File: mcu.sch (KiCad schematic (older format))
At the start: 73 parts, among them J10 JTAG, J11 esp32L, J12 esp32B, J13 esp32R, J2 SPI1, J3 uSD, J4 I2C1, J5 serial1, J6 serial2, J7 touch interface, J8 LCD 4.3, J9 EXT_IOS, Q1 ZXMN2F30FH, Q2 ZXMN2F30FH, Q3 ZXMN2F30FH, SW1 reset, SW7 on, U3 AT25SF641, U5 STM32F750Z8, U6 MP3302DJ-LF-P, U7 ESP32-WROOM-32, Y1 25MHz, Y2 32.768 kHz

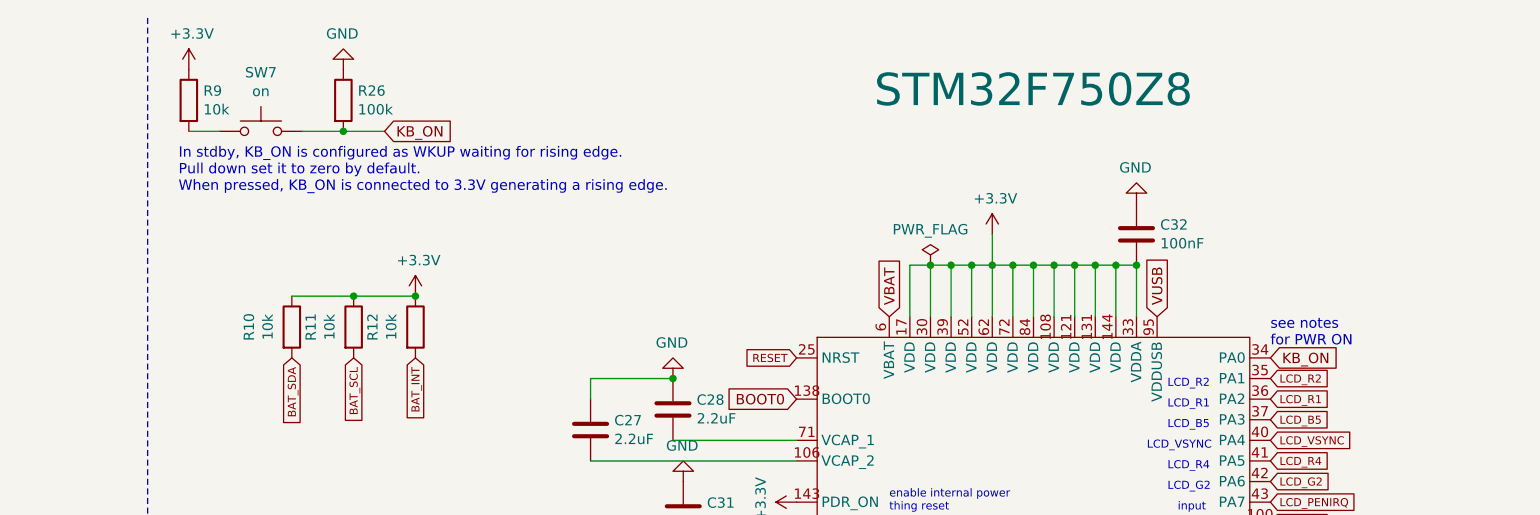
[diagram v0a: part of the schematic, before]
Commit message: fix wakeup
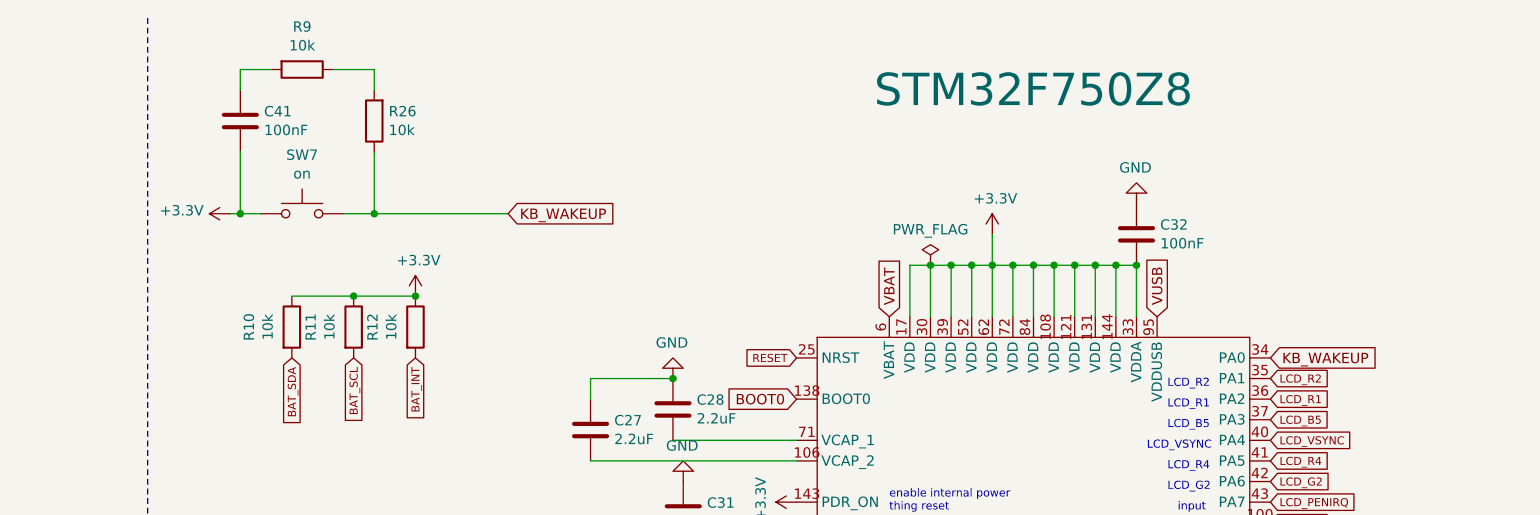
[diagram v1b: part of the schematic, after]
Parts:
- added C41: 100nF, Capacitor_SMD:C_0805_2012Metric_Pad1.18x1.45mm_HandSolder, symbol Device:C
- R26: value 100k -> 10k
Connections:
- net +3V3: now also SW7.1, C41.1; no longer R9.1
- net GND: no longer R26.1
- net at R9.2: now also C41.2; no longer SW7.1
- net KB_ON renamed KB_WAKEUP
- net KB_WAKEUP: now also R26.1; no longer R26.2
- new net: R26.2, R9.1
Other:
- note removed: "In stdby, KB_ON is configured as WKUP waiting for rising edge.\nPull down set it to zero by default.\nWhen pressed, KB_ON is connected to 3.3V generating a rising edge."
- note removed: "see notes\nfor PWR ON"
- moved on the sheet: SW7
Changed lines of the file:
@@
 KB_ROW_10
 Text GLabel 15050 2150 2    50   Input ~ 0
-KB_ON
+KB_WAKEUP
 Text Notes 3750 10750 0    118  ~ 0
 PWR On button is KB_COL_1 / KB_ROW_11\nESC button is KB_COL_12 / KB_ROW_1
@@
 Text Notes 600  11100 0    98   ~ 0
 TODO to validate:\n- BOOT0 behavior\n- WAKEUP through ON behavior\n- RESET
-Text Notes 15050 2100 0    50   ~ 0
-see notes\nfor PWR ON
 Text Notes 15500 4300 0    39   ~ 0
 TIM3_CH1
@@
 Text Notes 10550 10900 0    39   ~ 0
 R VF=1.8-2.4 FC=30\nG VF=2.8-3.9 FC=20\nB VF=2.8-3.9 FC=20\nSupply=3.3
-Text GLabel 10750 1050 2    50   Input ~ 0
-KB_ON
+Text GLabel 11350 1450 2    50   Input ~ 0
+KB_WAKEUP
 $Comp
 L Switch:SW_Push SW7
 U 1 1 5F9751F4
-P 10150 1050
-F 0 "SW7" H 10150 1335 50  0000 C CNN
-F 1 "on" H 10150 1244 50  0000 C CNN
-F 2 "Button_Switch_THT:SW_PUSH_6mm" H 10150 1250 50  0001 C CNN
-F 3 "~" H 10150 1250 50  0001 C CNN
-	1    10150 1050
-	1    0    0    -1
-$EndComp
-$Comp
-L Device:R R26
-U 1 1 5F97E218
-P 10550 900
-F 0 "R26" H 10620 946 50  0000 L CNN
-F 1 "100k" H 10620 855 50  0000 L CNN
-F 2 "Resistor_SMD:R_0805_2012Metric_Pad1.20x1.40mm_HandSolder" V 10480 900 50  0001 C CNN
-F 3 "~" H 10550 900 50  0001 C CNN
-	1    10550 900
-	1    0    0    -1
-$EndComp
-Wire Wire Line
-	10350 1050 10550 1050
-Connection ~ 10550 1050
-Wire Wire Line
-	10550 1050 10750 1050
-$Comp
-L power:GND #PWR0111
-U 1 1 5F98559E
-P 10550 750
-F 0 "#PWR0111" H 10550 500 50  0001 C CNN
-F 1 "GND" H 10555 577 50  0000 C CNN
-F 2 "" H 10550 750 50  0001 C CNN
-F 3 "" H 10550 750 50  0001 C CNN
-	1    10550 750
-	-1   0    0    1
-$EndComp
-$Comp
-L Device:R R9
-U 1 1 5F987D50
-P 9800 900
-F 0 "R9" H 9870 946 50  0000 L CNN
-F 1 "10k" H 9870 855 50  0000 L CNN
-F 2 "Resistor_SMD:R_0805_2012Metric_Pad1.20x1.40mm_HandSolder" V 9730 900 50  0001 C CNN
-F 3 "~" H 9800 900 50  0001 C CNN
-	1    9800 900
-	1    0    0    -1
-$EndComp
-Wire Wire Line
-	9800 1050 9950 1050
-$Comp
-L power:+3.3V #PWR0125
-U 1 1 5F98FA73
-P 9800 750
-F 0 "#PWR0125" H 9800 600 50  0001 C CNN
-F 1 "+3.3V" H 9815 923 50  0000 C CNN
-F 2 "" H 9800 750 50  0001 C CNN
-F 3 "" H 9800 750 50  0001 C CNN
-	1    9800 750
-	1    0    0    -1
-$EndComp
-Text Notes 9750 1350 0    50   ~ 0
-In stdby, KB_ON is configured as WKUP waiting for rising edge.\nPull down set it to zero by default.\nWhen pressed, KB_ON is connected to 3.3V generating a rising edge.
+P 10350 1450
+F 0 "SW7" H 10350 1735 50  0000 C CNN
+F 1 "on" H 10350 1644 50  0000 C CNN
+F 2 "Button_Switch_THT:SW_PUSH_6mm" H 10350 1650 50  0001 C CNN
+F 3 "~" H 10350 1650 50  0001 C CNN
+	1    10350 1450
+	1    0    0    -1
+$EndComp
 Text Notes 9650 3500 0    59   ~ 0
 internal i2c:\n6BH - Battery charger\nBA/BB or 28/29 - Touch display\n20 - Keyboard matrix output
+$Comp
+L power:+3.3V #PWR0111
+U 1 1 5FA49B5B
+P 10000 1450
+F 0 "#PWR0111" H 10000 1300 50  0001 C CNN
+F 1 "+3.3V" V 10015 1578 50  0000 L CNN
+F 2 "" H 10000 1450 50  0001 C CNN
+F 3 "" H 10000 1450 50  0001 C CNN
+	1    10000 1450
+	0    -1   -1   0
+$EndComp
+$Comp
+L Device:C C41
+U 1 1 5FA4B68A
+P 10050 1000
+F 0 "C41" H 9935 954 50  0000 R CNN
+F 1 "100nF" H 9935 1045 50  0000 R CNN
+F 2 "Capacitor_SMD:C_0805_2012Metric_Pad1.18x1.45mm_HandSolder" H 10088 850 50  0001 C CNN
+F 3 "~" H 10050 1000 50  0001 C CNN
+	1    10050 1000
+	-1   0    0    1
+$EndComp
+$Comp
+L Device:R R26
+U 1 1 5FA5B33C
+P 10700 1000
+F 0 "R26" H 10630 954 50  0000 R CNN
+F 1 "10k" H 10630 1045 50  0000 R CNN
+F 2 "Resistor_SMD:R_0805_2012Metric_Pad1.20x1.40mm_HandSolder" V 10630 1000 50  0001 C CNN
+F 3 "~" H 10700 1000 50  0001 C CNN
+	1    10700 1000
+	-1   0    0    1
+$EndComp
+$Comp
+L Device:R R9
+U 1 1 5FA5CDAE
+P 10350 750
+F 0 "R9" V 10143 750 50  0000 C CNN
+F 1 "10k" V 10234 750 50  0000 C CNN
+F 2 "Resistor_SMD:R_0805_2012Metric_Pad1.20x1.40mm_HandSolder" V 10280 750 50  0001 C CNN
+F 3 "~" H 10350 750 50  0001 C CNN
+	1    10350 750
+	0    1    1    0
+$EndComp
+Wire Wire Line
+	10000 1450 10050 1450
+Wire Wire Line
+	10550 1450 10700 1450
+Wire Wire Line
+	10500 750  10700 750
+Wire Wire Line
+	10700 750  10700 850
+Wire Wire Line
+	10700 1150 10700 1450
+Connection ~ 10700 1450
+Wire Wire Line
+	10700 1450 11350 1450
+Wire Wire Line
+	10050 1450 10050 1150
+Connection ~ 10050 1450
+Wire Wire Line
+	10050 1450 10150 1450
+Wire Wire Line
+	10050 850  10050 750
+Wire Wire Line
+	10050 750  10200 750
 $EndSCHEMATC

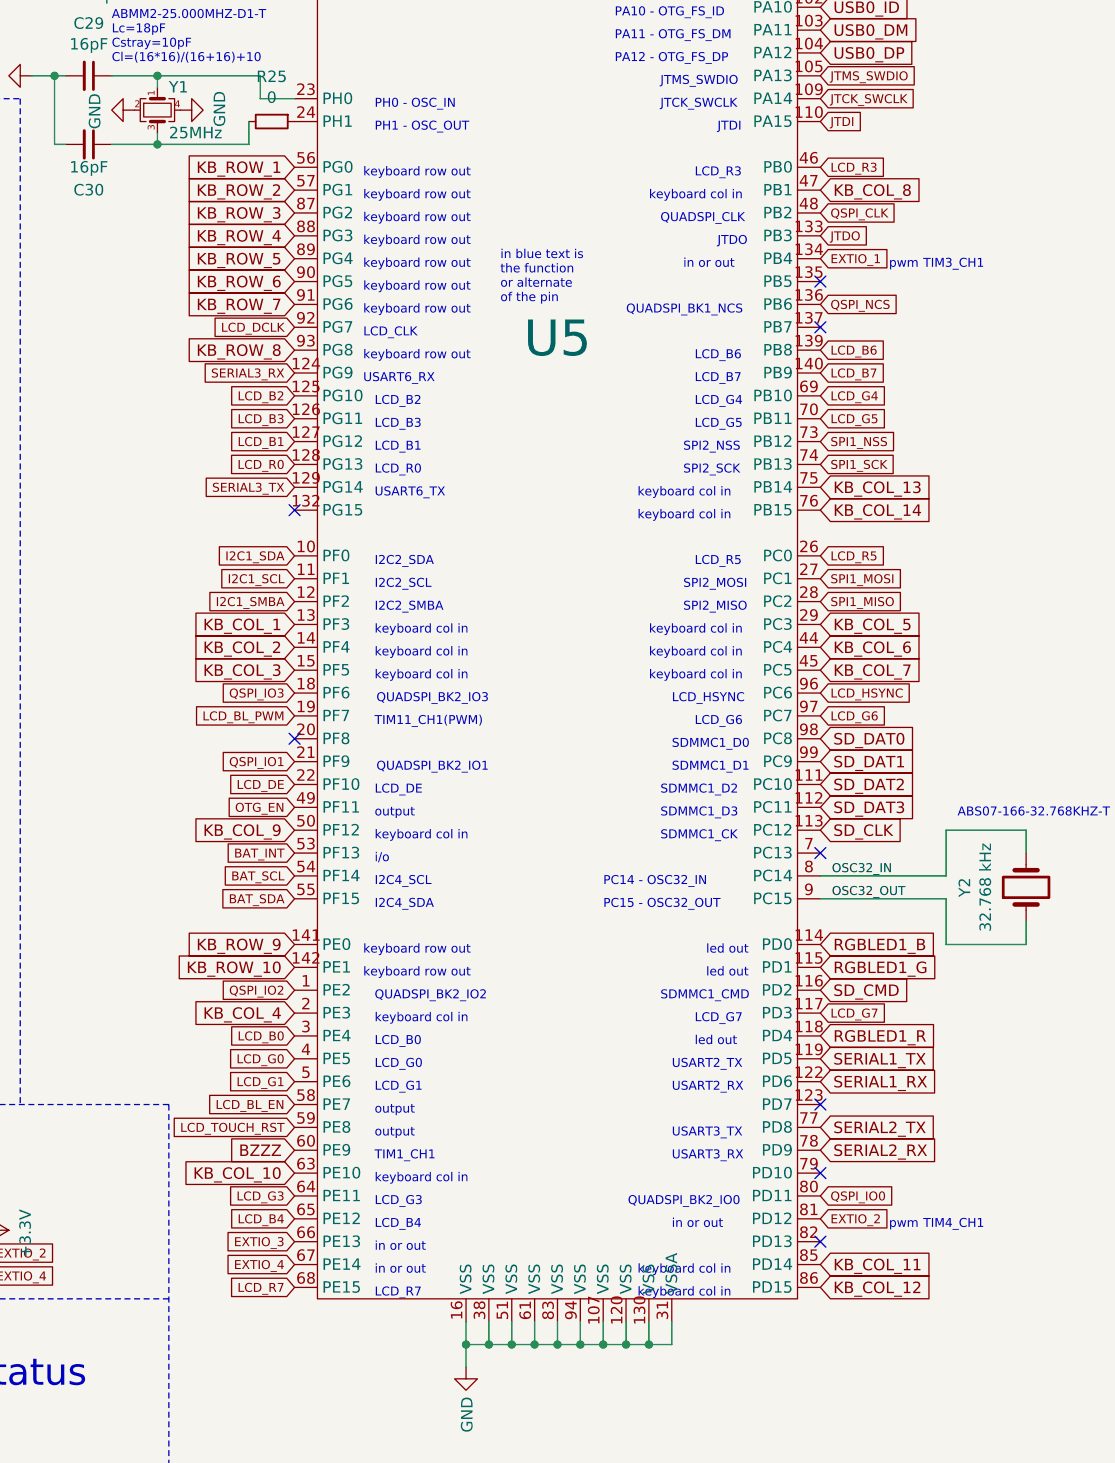
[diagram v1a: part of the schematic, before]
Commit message: frees mcu pins
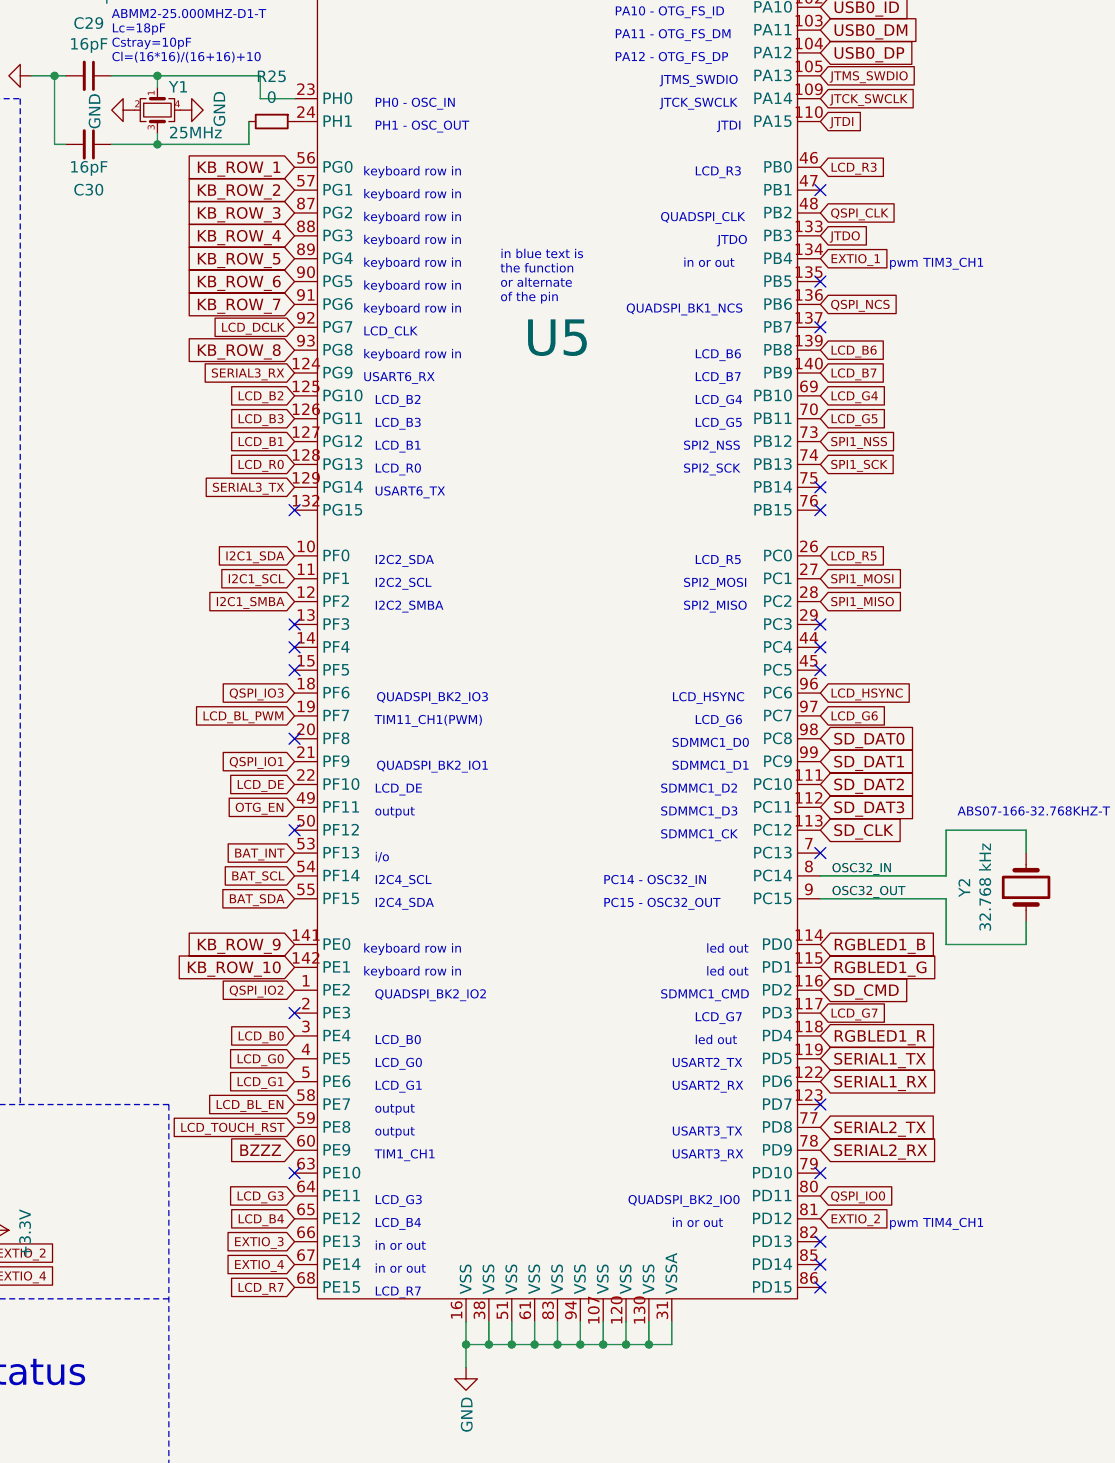
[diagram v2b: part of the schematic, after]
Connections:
- net KB_COL_12: no longer U5.86 (PD15)
- net KB_COL_1: no longer names the net of U5.13 (PF3)
- net KB_COL_10: no longer names the net of U5.63 (PE10)
- net KB_COL_11: no longer names the net of U5.85 (PD14)
- net KB_COL_13: no longer names the net of U5.75 (PB14)
- net KB_COL_14: no longer names the net of U5.76 (PB15)
- net KB_COL_2: no longer names the net of U5.14 (PF4)
- net KB_COL_3: no longer names the net of U5.15 (PF5)
- net KB_COL_4: no longer names the net of U5.2 (PE3)
- net KB_COL_5: no longer names the net of U5.29 (PC3)
- net KB_COL_6: no longer names the net of U5.44 (PC4)
- net KB_COL_7: no longer names the net of U5.45 (PC5)
- net KB_COL_8: no longer names the net of U5.47 (PB1)
- net KB_COL_9: no longer names the net of U5.50 (PF12)
- no-connect marks 15 -> 29
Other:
- note added: "keyboard row in"
- note removed: "keyboard col in"
- note removed: "keyboard row out"
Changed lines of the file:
@@
 	1    0    0    -1
 $EndComp
-Text GLabel 12750 8250 0    50   Input ~ 0
-KB_COL_10
-Text GLabel 12750 6750 0    50   Input ~ 0
-KB_COL_9
-Text GLabel 15050 3950 2    50   Input ~ 0
-KB_COL_8
-Text GLabel 15050 6050 2    50   Input ~ 0
-KB_COL_7
-Text GLabel 15050 5950 2    50   Input ~ 0
-KB_COL_6
-Text GLabel 15050 5850 2    50   Input ~ 0
-KB_COL_5
-Text GLabel 12750 7550 0    50   Input ~ 0
-KB_COL_4
-Text GLabel 12750 6050 0    50   Input ~ 0
-KB_COL_3
-Text GLabel 12750 5950 0    50   Input ~ 0
-KB_COL_2
-Text GLabel 12750 5850 0    50   Input ~ 0
-KB_COL_1
-Text GLabel 15050 8650 2    50   Input ~ 0
-KB_COL_11
-Text GLabel 15050 8750 2    50   Input ~ 0
-KB_COL_12
-Text GLabel 15050 5250 2    50   Input ~ 0
-KB_COL_13
-Text GLabel 15050 5350 2    50   Input ~ 0
-KB_COL_14
 Text GLabel 12750 4650 0    50   Input ~ 0
 KB_ROW_8
@@
 COL are inputs, pull-up sw\nROW output
 Text Notes 13050 3900 0    39   ~ 0
-keyboard row out
+keyboard row in
 Text Notes 13050 4000 0    39   ~ 0
-keyboard row out
+keyboard row in
 Text Notes 13050 4100 0    39   ~ 0
-keyboard row out
+keyboard row in
 Text Notes 13050 4200 0    39   ~ 0
-keyboard row out
+keyboard row in
 Text Notes 13050 4300 0    39   ~ 0
-keyboard row out
+keyboard row in
 Text Notes 13050 4400 0    39   ~ 0
-keyboard row out
+keyboard row in
 Text Notes 13050 4500 0    39   ~ 0
-keyboard row out
+keyboard row in
 Text Notes 13050 7300 0    39   ~ 0
-keyboard row out
+keyboard row in
 Text Notes 13050 4700 0    39   ~ 0
-keyboard row out
+keyboard row in
 Text Notes 13050 7400 0    39   ~ 0
-keyboard row out
-Text Notes 13100 5900 0    39   ~ 0
-keyboard col in
-Text Notes 13100 6000 0    39   ~ 0
-keyboard col in
-Text Notes 13100 6100 0    39   ~ 0
-keyboard col in
-Text Notes 14300 4000 0    39   ~ 0
-keyboard col in
-Text Notes 13100 6800 0    39   ~ 0
-keyboard col in
-Text Notes 14250 5300 0    39   ~ 0
-keyboard col in
-Text Notes 14250 5400 0    39   ~ 0
-keyboard col in
-Text Notes 14300 5900 0    39   ~ 0
-keyboard col in
-Text Notes 14250 8700 0    39   ~ 0
-keyboard col in
-Text Notes 14300 6000 0    39   ~ 0
-keyboard col in
-Text Notes 14300 6100 0    39   ~ 0
-keyboard col in
-Text Notes 14250 8800 0    39   ~ 0
-keyboard col in
-Text Notes 13100 7600 0    39   ~ 0
-keyboard col in
-Text Notes 13100 8300 0    39   ~ 0
-keyboard col in
+keyboard row in
 Text GLabel 12750 4750 0    39   Input ~ 0
 SERIAL3_RX
@@
 Wire Wire Line
 	10050 750  10200 750
+NoConn ~ 15050 5250
+NoConn ~ 15050 5350
+NoConn ~ 15050 5850
+NoConn ~ 15050 5950
+NoConn ~ 15050 6050
+NoConn ~ 12750 5850
+NoConn ~ 12750 5950
+NoConn ~ 12750 6050
+NoConn ~ 12750 7550
+NoConn ~ 12750 8250
+NoConn ~ 15050 8650
+NoConn ~ 15050 8750
+NoConn ~ 15050 3950
+NoConn ~ 12750 6750
 $EndSCHEMATC
